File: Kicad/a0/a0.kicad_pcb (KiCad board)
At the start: 2 copper layers, 190 x 100 mm, 73 parts, among them J1 Conn_02x03_Odd_Even, J2 VGA, J4 AudioJack3_SwitchTR, J5 Conn_02x17_Odd_Even, J6 Barrel_Jack_MountingPin, J7 DE9_Plug, J8 DE9_Plug, SW1 SW_Push_45deg, SW10 SW_Push_45deg, SW11 SW_Push_45deg, SW12 SW_Push_45deg, SW13 SW_Push_45deg, SW14 SW_Push_45deg, SW15 SW_Push_45deg, SW16 SW_Push_45deg, SW17 SW_Push_45deg, SW18 SW_Push_45deg, SW19 SW_Push_45deg, SW2 SW_Push_45deg, SW20 SW_Push_45deg, SW21 SW_Push_45deg, SW22 SW_Push_45deg, SW23 SW_Push_45deg, SW24 SW_Push_45deg, SW25 SW_Push_45deg, SW26 SW_Push_45deg, SW27 SW_Push_45deg, SW28 SW_Push_45deg, SW29 SW_Push_45deg, SW3 SW_Push_45deg, SW30 SW_Push_45deg, SW31 SW_Push, SW32 SW_SPDT, SW4 SW_Push_45deg, SW5 SW_Push_45deg, SW6 SW_Push_45deg, SW7 SW_Push_45deg, SW8 SW_Push_45deg, SW9 SW_Push_45deg, U1 74HC590A, U10 74LS541, U11 74LS166, U2 74HC590A, U3 74LS14, U4 74LS174, U5 4520, U6 74LS32, U7 74LS10, U8 CY62256-70PC, U9 28C256, Y1 Crystal

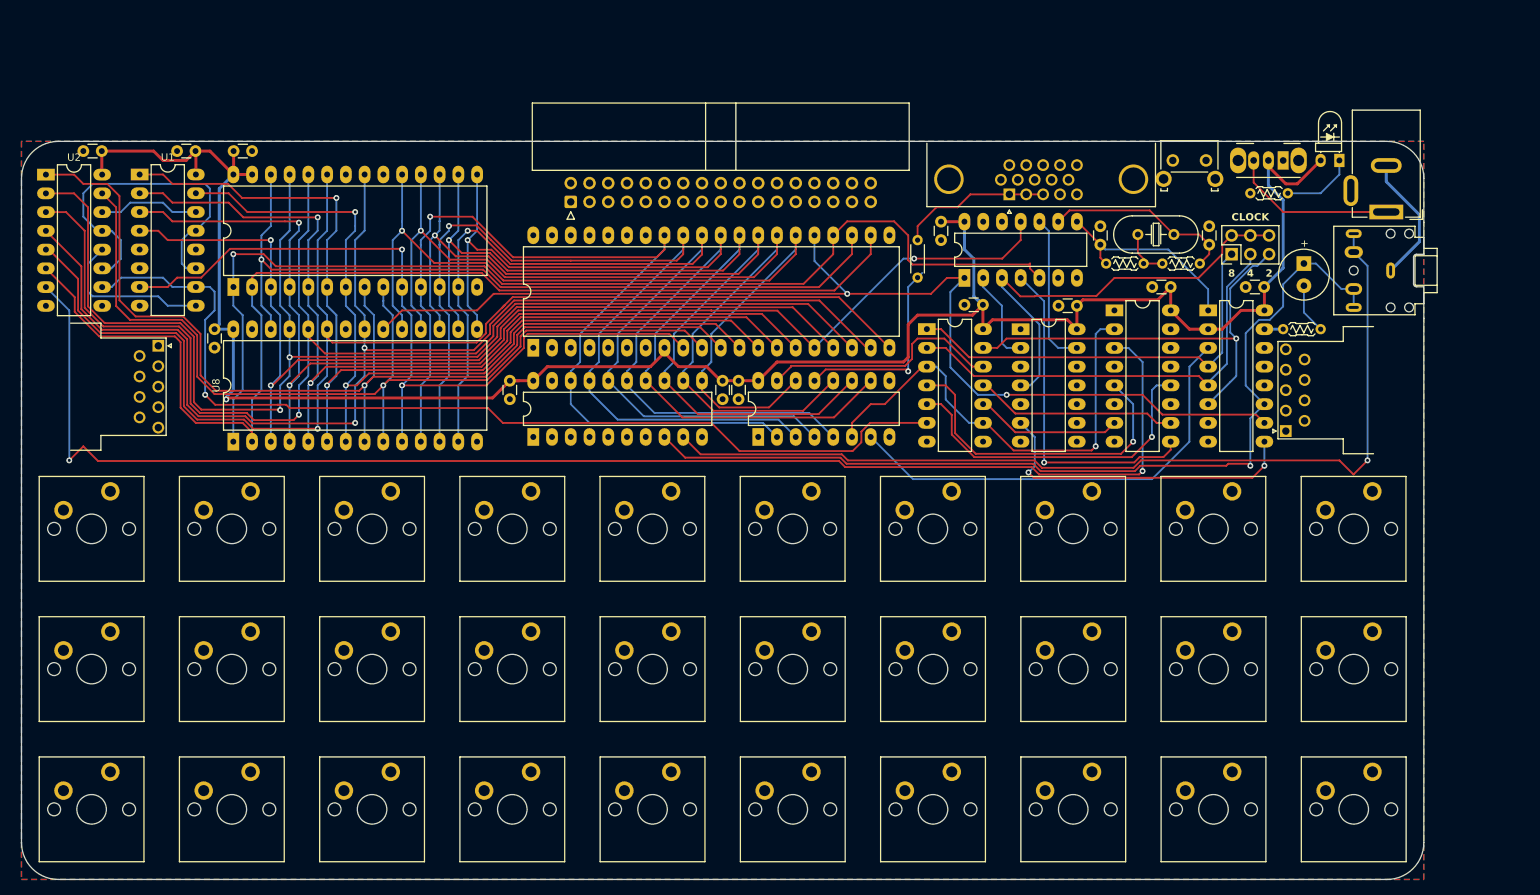
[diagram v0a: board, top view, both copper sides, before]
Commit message: pcb,bios,font  improvements
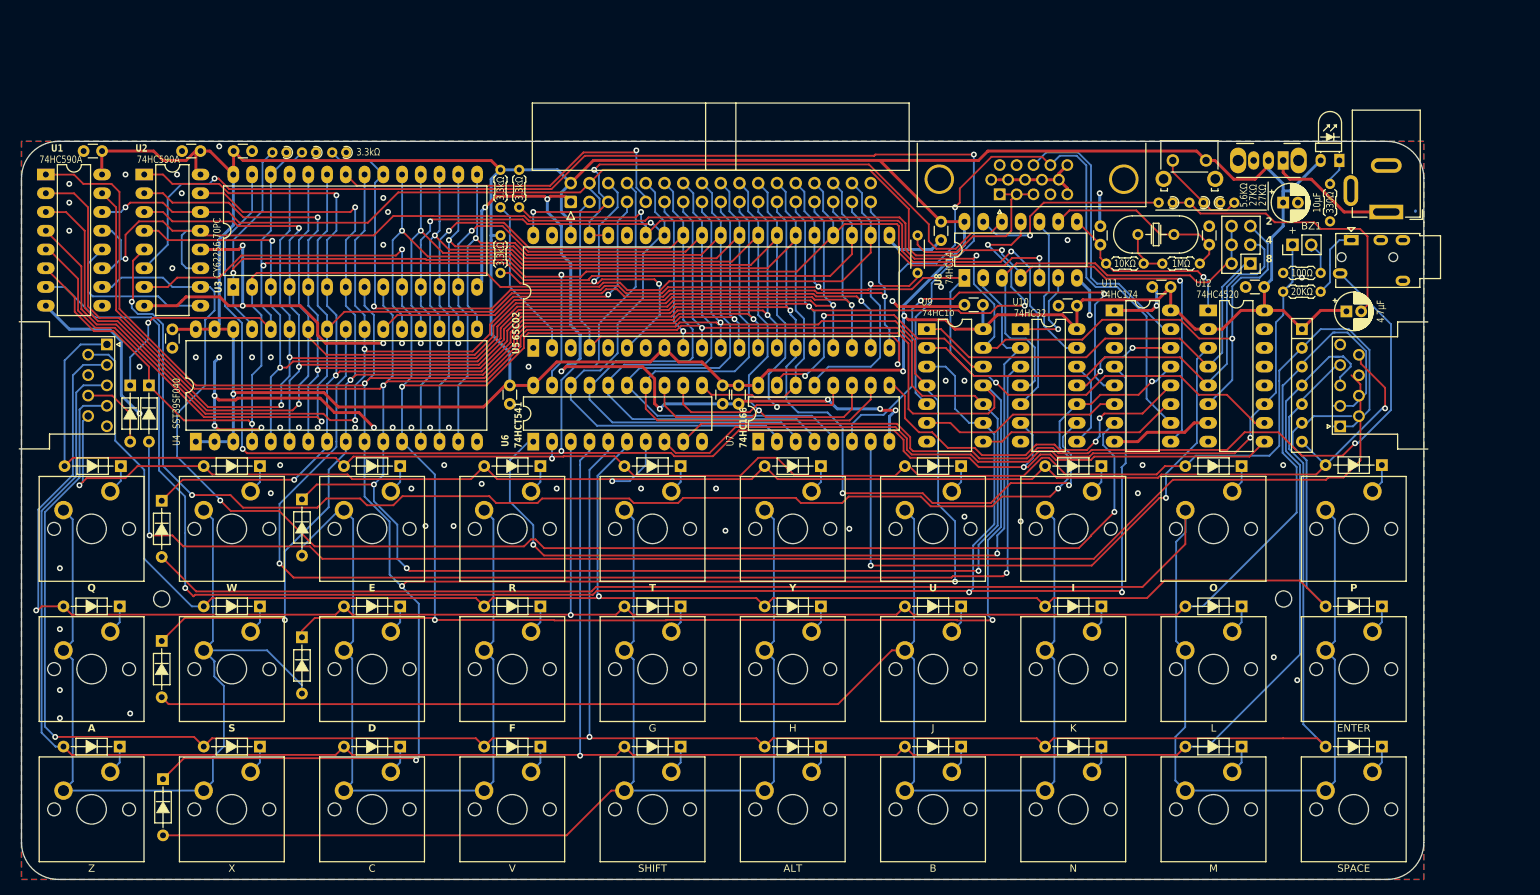
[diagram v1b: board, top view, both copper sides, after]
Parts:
- removed J4: AudioJack3_SwitchTR, Connector_Audio:Jack_3.5mm_CUI_SJ1-3525N_Horizontal
- removed the U9 at (76.2, 62.2)
- added C16: 10µF, PCM_Capacitor_THT_AKL:CP_Radial_D5.0mm_P2.00mm, F.Cu at (218.4, 50.8)
- added C3: 4.7µF, PCM_Capacitor_THT_AKL:CP_Radial_D5.0mm_P2.00mm, F.Cu at (227.0, 65.5)
- added D10: 1N4148, PCM_Diode_THT_AKL:D_DO-35_SOD27_P7.62mm_Horizontal, F.Cu at (174.8, 86.5)
- added D11: 1N4148, PCM_Diode_THT_AKL:D_DO-35_SOD27_P7.62mm_Horizontal, F.Cu at (212.8, 86.5)
- added D12: 1N4148, PCM_Diode_THT_AKL:D_DO-35_SOD27_P7.62mm_Horizontal, F.Cu at (231.8, 86.4)
- added D13: 1N4148, PCM_Diode_THT_AKL:D_DO-35_SOD27_P7.62mm_Horizontal, F.Cu at (193.8, 86.5)
- added D14: 1N4148, PCM_Diode_THT_AKL:D_DO-35_SOD27_P7.62mm_Horizontal, F.Cu at (155.8, 86.5)
- added D15: 1N4148, PCM_Diode_THT_AKL:D_DO-35_SOD27_P7.62mm_Horizontal, F.Cu at (117.8, 86.5)
- added D16: 1N4148, PCM_Diode_THT_AKL:D_DO-35_SOD27_P7.62mm_Horizontal, F.Cu at (79.8, 86.5)
- added D17: 1N4148, PCM_Diode_THT_AKL:D_DO-35_SOD27_P7.62mm_Horizontal, F.Cu at (60.8, 105.5)
- added D18: 1N4148, PCM_Diode_THT_AKL:D_DO-35_SOD27_P7.62mm_Horizontal, F.Cu at (98.8, 105.5)
- added D19: 1N4148, PCM_Diode_THT_AKL:D_DO-35_SOD27_P7.62mm_Horizontal, F.Cu at (136.8, 105.5)
- added D2: 1N4148, PCM_Diode_THT_AKL:D_DO-35_SOD27_P7.62mm_Horizontal, F.Cu at (85.5, 109.7)
- added D20: 1N4148, PCM_Diode_THT_AKL:D_DO-35_SOD27_P7.62mm_Horizontal, F.Cu at (174.8, 105.5)
- added D21: 1N4148, PCM_Diode_THT_AKL:D_DO-35_SOD27_P7.62mm_Horizontal, F.Cu at (212.8, 105.5)
- added D22: 1N4148, PCM_Diode_THT_AKL:D_DO-35_SOD27_P7.62mm_Horizontal, F.Cu at (79.8, 105.5)
- added D23: 1N4148, PCM_Diode_THT_AKL:D_DO-35_SOD27_P7.62mm_Horizontal, F.Cu at (117.8, 105.5)
- added D24: 1N4148, PCM_Diode_THT_AKL:D_DO-35_SOD27_P7.62mm_Horizontal, F.Cu at (155.8, 105.5)
- added D25: 1N4148, PCM_Diode_THT_AKL:D_DO-35_SOD27_P7.62mm_Horizontal, F.Cu at (193.8, 105.5)
- added D26: 1N4148, PCM_Diode_THT_AKL:D_DO-35_SOD27_P7.62mm_Horizontal, F.Cu at (231.8, 105.5)
- added D27: 1N4148, PCM_Diode_THT_AKL:D_DO-35_SOD27_P7.62mm_Horizontal, F.Cu at (60.8, 124.5)
- added D28: 1N4148, PCM_Diode_THT_AKL:D_DO-35_SOD27_P7.62mm_Horizontal, F.Cu at (98.8, 124.5)
- added D29: 1N4148, PCM_Diode_THT_AKL:D_DO-35_SOD27_P7.62mm_Horizontal, F.Cu at (136.8, 124.5)
- added D3: 1N4148, PCM_Diode_THT_AKL:D_DO-35_SOD27_P7.62mm_Horizontal, F.Cu at (85.5, 91.0)
- added D30: 1N4148, PCM_Diode_THT_AKL:D_DO-35_SOD27_P7.62mm_Horizontal, F.Cu at (174.8, 124.5)
- added D31: 1N4148, PCM_Diode_THT_AKL:D_DO-35_SOD27_P7.62mm_Horizontal, F.Cu at (212.8, 124.5)
- added D32: 1N4148, PCM_Diode_THT_AKL:D_DO-35_SOD27_P7.62mm_Horizontal, F.Cu at (79.8, 124.5)
- added D33: 1N4148, PCM_Diode_THT_AKL:D_DO-35_SOD27_P7.62mm_Horizontal, F.Cu at (117.8, 124.5)
- added D34: 1N4148, PCM_Diode_THT_AKL:D_DO-35_SOD27_P7.62mm_Horizontal, F.Cu at (155.8, 124.5)
- added D35: 1N4148, PCM_Diode_THT_AKL:D_DO-35_SOD27_P7.62mm_Horizontal, F.Cu at (193.8, 124.5)
- added D36: 1N4148, PCM_Diode_THT_AKL:D_DO-35_SOD27_P7.62mm_Horizontal, F.Cu at (231.8, 124.5)
- added D37: 1N4148, PCM_Diode_THT_AKL:D_DO-35_SOD27_P7.62mm_Horizontal, F.Cu at (64.8, 75.6)
- added D38: 1N4148, PCM_Diode_THT_AKL:D_DO-35_SOD27_P7.62mm_Horizontal, F.Cu at (62.2, 75.6)
- added D4: 1N4148, PCM_Diode_THT_AKL:D_DO-35_SOD27_P7.62mm_Horizontal, F.Cu at (66.7, 128.9)
- added D5: 1N4148, PCM_Diode_THT_AKL:D_DO-35_SOD27_P7.62mm_Horizontal, F.Cu at (66.5, 110.2)
- added D6: 1N4148, PCM_Diode_THT_AKL:D_DO-35_SOD27_P7.62mm_Horizontal, F.Cu at (66.5, 91.2)
- added D7: 1N4148, PCM_Diode_THT_AKL:D_DO-35_SOD27_P7.62mm_Horizontal, F.Cu at (61.0, 86.5)
- added D8: 1N4148, PCM_Diode_THT_AKL:D_DO-35_SOD27_P7.62mm_Horizontal, F.Cu at (98.8, 86.5)
- added D9: 1N4148, PCM_Diode_THT_AKL:D_DO-35_SOD27_P7.62mm_Horizontal, F.Cu at (136.8, 86.5)
- added H1: MountingHole, MountingHole:MountingHole_2.2mm_M2, F.Cu at (66.5, 104.5)
- added H2: MountingHole, MountingHole:MountingHole_2.2mm_M2, F.Cu at (218.5, 104.5)
- added J3: AudioJack4, Connector_Audio:Jack_3.5mm_PJ320E_Horizontal, F.Cu at (227.7, 55.9)
- added R10: 3.3kΩ, PCM_Resistor_THT_AKL:R_Axial_DIN0204_L3.6mm_D1.6mm_P5.08mm_Horizontal, F.Cu at (114.9, 46.4)
- added R11: 5.6KΩ, PCM_Resistor_THT_US_AKL:R_Axial_DIN0204_L3.6mm_D1.6mm_P1.90mm_Vertical, F.Cu at (203.5, 50.8)
- added R12: 27KΩ, PCM_Resistor_THT_US_AKL:R_Axial_DIN0204_L3.6mm_D1.6mm_P1.90mm_Vertical, F.Cu at (207.6, 50.8)
- added R13: 27KΩ, PCM_Resistor_THT_US_AKL:R_Axial_DIN0204_L3.6mm_D1.6mm_P1.90mm_Vertical, F.Cu at (209.9, 50.8)
- added R14: 20KΩ, PCM_Resistor_THT_AKL:R_Axial_DIN0204_L3.6mm_D1.6mm_P5.08mm_Horizontal, F.Cu at (218.4, 62.9)
- added R15: 3.3kΩ, PCM_Resistor_THT_AKL:R_Axial_DIN0204_L3.6mm_D1.6mm_P5.08mm_Horizontal, F.Cu at (112.4, 55.2)
- added R6: R_Small, PCM_Resistor_THT_AKL:R_Axial_DIN0204_L3.6mm_D1.6mm_P1.90mm_Vertical, F.Cu at (91.5, 44.0)
- added R7: R_Small, PCM_Resistor_THT_AKL:R_Axial_DIN0204_L3.6mm_D1.6mm_P1.90mm_Vertical, F.Cu at (83.4, 44.0)
- added R8: R_Small, PCM_Resistor_THT_AKL:R_Axial_DIN0204_L3.6mm_D1.6mm_P1.90mm_Vertical, F.Cu at (87.4, 44.0)
- added R9: 3.3kΩ, PCM_Resistor_THT_AKL:R_Axial_DIN0204_L3.6mm_D1.6mm_P5.08mm_Horizontal, F.Cu at (112.4, 46.4)
- added RN1: R_Network06, Resistor_THT:R_Array_SIP7, F.Cu at (221.0, 67.9)
- added U4: SST39SF040, Package_DIP:DIP-32_W15.24mm_LongPads, F.Cu at (71.1, 83.2)
- BZ1: footprint Buzzer_Beeper:MagneticBuzzer_Kobitone_254-EMB73-RO -> Connector_PinHeader_2.54mm:PinHeader_1x02_P2.54mm_Vertical
- J6: value Barrel_Jack_MountingPin -> Barrel Jack
- R1: value R -> 1MΩ; footprint PCM_Resistor_THT_US_AKL_Double:R_Axial_DIN0204_L3.6mm_D1.6mm_P5.08mm_Horizontal -> PCM_Resistor_THT_AKL:R_Axial_DIN0204_L3.6mm_D1.6mm_P5.08mm_Horizontal
- R2: value R -> 10KΩ; footprint PCM_Resistor_THT_US_AKL_Double:R_Axial_DIN0204_L3.6mm_D1.6mm_P5.08mm_Horizontal -> PCM_Resistor_THT_AKL:R_Axial_DIN0204_L3.6mm_D1.6mm_P5.08mm_Horizontal
- R4: value R -> 330Ω; footprint PCM_Resistor_THT_US_AKL_Double:R_Axial_DIN0204_L3.6mm_D1.6mm_P5.08mm_Horizontal -> PCM_Resistor_THT_AKL:R_Axial_DIN0204_L3.6mm_D1.6mm_P5.08mm_Horizontal
- R5: value R -> 100Ω; footprint PCM_Resistor_THT_US_AKL_Double:R_Axial_DIN0204_L3.6mm_D1.6mm_P5.08mm_Horizontal -> PCM_Resistor_THT_AKL:R_Axial_DIN0204_L3.6mm_D1.6mm_P5.08mm_Horizontal
- SW1: value SW_Push_45deg -> Q
- SW10: value SW_Push_45deg -> P
- SW11: value SW_Push_45deg -> A
- SW12: value SW_Push_45deg -> S
- SW13: value SW_Push_45deg -> D
- SW14: value SW_Push_45deg -> F
- SW15: value SW_Push_45deg -> G
- SW16: value SW_Push_45deg -> H
- SW17: value SW_Push_45deg -> J
- SW18: value SW_Push_45deg -> K
- SW19: value SW_Push_45deg -> L
- SW2: value SW_Push_45deg -> W
- SW20: value SW_Push_45deg -> ENTER
- SW21: value SW_Push_45deg -> Z
- SW22: value SW_Push_45deg -> X
- SW23: value SW_Push_45deg -> C
- SW24: value SW_Push_45deg -> V
- SW25: value SW_Push_45deg -> SHIFT
- SW26: value SW_Push_45deg -> ALT
- SW27: value SW_Push_45deg -> B
- SW28: value SW_Push_45deg -> N
- SW29: value SW_Push_45deg -> M
- SW3: value SW_Push_45deg -> E
- SW30: value SW_Push_45deg -> SPACE
- SW4: value SW_Push_45deg -> R
- SW5: value SW_Push_45deg -> T
- SW6: value SW_Push_45deg -> Y
- SW7: value SW_Push_45deg -> U
- SW8: value SW_Push_45deg -> I
- SW9: value SW_Push_45deg -> O
- U10: renamed from U6; value 74LS32 -> 74HC32
- U11: renamed from U4; value 74LS174 -> 74HC174
- U12: renamed from U5; value 4520 -> 74HC4520
- U5: renamed from U12; value ~ -> 65C02
- U6: renamed from U10; value 74LS541 -> 74HCT541
- U7: renamed from U11; value 74LS166 -> 74HC166
- U8: renamed from U3; value 74LS14 -> 74HC14
- U9: renamed from U7; value 74LS10 -> 74HC10
- Y1: value Crystal -> 32Mhz
- moved J8 160.5 mm to (226.2, 81.1), turned to 90 degrees
- moved J7 160.2 mm to (59.1, 70.0), turned to -90 degrees
- moved U3 21.0 mm to (76.2, 62.2)
- moved R4 11.4 mm to (224.8, 53.3), turned to 90 degrees
- moved R5 7.62 mm to (223.5, 60.3)
- moved C7 5.72 mm to (67.9, 70.5)
- moved BZ1 2.97 mm to (219.7, 56.5), turned to 90 degrees
- moved J1 2.84 mm to (214.0, 59.1), turned to 180 degrees
- moved J2 1.31 mm to (180.0, 49.7)
- moved C5 0.67 mm to (69.3, 43.8)
- moved U6 0.64 mm to (116.8, 83.2)
- moved U7 0.64 mm to (147.3, 83.2)
- moved R3 0.63 mm to (168.9, 60.3)
- moved C10 0.63 mm to (144.7, 78.1)
- moved C8 0.63 mm to (113.7, 78.1)
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- renumbered U2 to U1, U1 to U2, U8 to U3
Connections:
- C10 pad 1: unconnected-(C10-Pad1) -> GND
- C11 pad 1: unconnected-(C11-Pad1) -> GND
- C12 pad 1: unconnected-(C12-Pad1) -> GND
- C13 pad 1: unconnected-(C13-Pad1) -> GND
- C14 pad 1: unconnected-(C14-Pad1) -> GND
- C15 pad 1: unconnected-(C15-Pad1) -> GND
- C4 pad 1: unconnected-(C4-Pad1) -> GND
- C5 pad 1: unconnected-(C5-Pad1) -> GND
- C6 pad 1: unconnected-(C6-Pad1) -> GND
- C7 pad 1: unconnected-(C7-Pad1) -> GND
- C8 pad 1: unconnected-(C8-Pad1) -> GND
- J5 pad 1: unconnected-(J5-Pin_1-Pad1) -> GND
- J5 pad 10: unconnected-(J5-Pin_10-Pad10) -> /D0
- J5 pad 11: unconnected-(J5-Pin_11-Pad11) -> /A0
- J5 pad 12: unconnected-(J5-Pin_12-Pad12) -> /D1
- J5 pad 13: unconnected-(J5-Pin_13-Pad13) -> /A1
- J5 pad 14: unconnected-(J5-Pin_14-Pad14) -> /D2
- J5 pad 15: unconnected-(J5-Pin_15-Pad15) -> /A2
- J5 pad 16: unconnected-(J5-Pin_16-Pad16) -> /D3
- J5 pad 17: unconnected-(J5-Pin_17-Pad17) -> /A3
- J5 pad 18: unconnected-(J5-Pin_18-Pad18) -> /D4
- J5 pad 19: unconnected-(J5-Pin_19-Pad19) -> /A4
- J5 pad 2: unconnected-(J5-Pin_2-Pad2) -> VCC
- J5 pad 20: unconnected-(J5-Pin_20-Pad20) -> /D5
- J5 pad 21: unconnected-(J5-Pin_21-Pad21) -> /A5
- J5 pad 22: unconnected-(J5-Pin_22-Pad22) -> /D6
- J5 pad 23: unconnected-(J5-Pin_23-Pad23) -> /A6
- J5 pad 24: unconnected-(J5-Pin_24-Pad24) -> /D7
- J5 pad 25: unconnected-(J5-Pin_25-Pad25) -> /A7
- J5 pad 26: unconnected-(J5-Pin_26-Pad26) -> /A15
- J5 pad 27: unconnected-(J5-Pin_27-Pad27) -> /A8
- J5 pad 28: unconnected-(J5-Pin_28-Pad28) -> /A14
- J5 pad 29: unconnected-(J5-Pin_29-Pad29) -> /A9
- J5 pad 3: unconnected-(J5-Pin_3-Pad3) -> /~{VSYNC}
- J5 pad 30: unconnected-(J5-Pin_30-Pad30) -> /A13
- J5 pad 31: unconnected-(J5-Pin_31-Pad31) -> /A10
- J5 pad 32: unconnected-(J5-Pin_32-Pad32) -> /A12
- J5 pad 33: unconnected-(J5-Pin_33-Pad33) -> /A11
- J5 pad 34: unconnected-(J5-Pin_34-Pad34) -> GND
- J5 pad 4: unconnected-(J5-Pin_4-Pad4) -> ø2
- J5 pad 5: unconnected-(J5-Pin_5-Pad5) -> /~{RESEŦ}
- J5 pad 6: unconnected-(J5-Pin_6-Pad6) -> /~{NMI}
- J5 pad 7: unconnected-(J5-Pin_7-Pad7) -> /ROMDIS
- J5 pad 8: unconnected-(J5-Pin_8-Pad8) -> /~{WR}
- J5 pad 9: unconnected-(J5-Pin_9-Pad9) -> /RAMDIS
- J6 pad 1: Net-(SW32-C) -> Net-(SW32-A)
- J7 pad 1: unconnected-(J7-Pad1) -> /HROW 0
- J7 pad 2: unconnected-(J7-Pad2) -> /HROW 1
- J7 pad 3: unconnected-(J7-Pad3) -> /HROW 2
- J7 pad 4: unconnected-(J7-Pad4) -> /HROW 3
- J7 pad 6: unconnected-(J7-Pad6) -> /HROW 4
- J7 pad 8: unconnected-(J7-Pad8) -> Net-(D38-A)
- J7 pad 9: unconnected-(J7-Pad9) -> /HROW 5
- J8 pad 1: unconnected-(J8-Pad1) -> /HROW 0
- J8 pad 2: unconnected-(J8-Pad2) -> /HROW 1
- J8 pad 3: unconnected-(J8-Pad3) -> /HROW 2
- J8 pad 4: unconnected-(J8-Pad4) -> /HROW 3
- J8 pad 6: unconnected-(J8-Pad6) -> /HROW 4
- J8 pad 8: unconnected-(J8-Pad8) -> Net-(D37-A)
- J8 pad 9: unconnected-(J8-Pad9) -> /HROW 5
- SW1 pad 1: unconnected-(SW1-Pad1) -> /COL 0
- SW1 pad 2: unconnected-(SW1-Pad2) -> Net-(D7-K)
- SW10 pad 1: unconnected-(SW10-Pad1) -> /COL 4
- SW10 pad 2: unconnected-(SW10-Pad2) -> Net-(D12-K)
- SW11 pad 1: unconnected-(SW11-Pad1) -> /COL 0
- SW11 pad 2: unconnected-(SW11-Pad2) -> Net-(D17-K)
- SW12 pad 1: unconnected-(SW12-Pad1) -> /COL 0
- SW12 pad 2: unconnected-(SW12-Pad2) -> Net-(D22-K)
- SW13 pad 1: unconnected-(SW13-Pad1) -> /COL 1
- SW13 pad 2: unconnected-(SW13-Pad2) -> Net-(D18-K)
- SW14 pad 1: unconnected-(SW14-Pad1) -> /COL 1
- SW14 pad 2: unconnected-(SW14-Pad2) -> Net-(D23-K)
- SW15 pad 1: unconnected-(SW15-Pad1) -> /COL 2
- SW15 pad 2: unconnected-(SW15-Pad2) -> Net-(D19-K)
- SW16 pad 1: unconnected-(SW16-Pad1) -> /COL 2
- SW16 pad 2: unconnected-(SW16-Pad2) -> Net-(D24-K)
- SW17 pad 1: unconnected-(SW17-Pad1) -> /COL 3
- SW17 pad 2: unconnected-(SW17-Pad2) -> Net-(D20-K)
- SW18 pad 1: unconnected-(SW18-Pad1) -> /COL 3
- SW18 pad 2: unconnected-(SW18-Pad2) -> Net-(D25-K)
- SW19 pad 1: unconnected-(SW19-Pad1) -> /COL 4
- SW19 pad 2: unconnected-(SW19-Pad2) -> Net-(D21-K)
- SW2 pad 1: unconnected-(SW2-Pad1) -> /COL 0
- SW2 pad 2: unconnected-(SW2-Pad2) -> Net-(D16-K)
- SW20 pad 1: unconnected-(SW20-Pad1) -> /COL 4
- SW20 pad 2: unconnected-(SW20-Pad2) -> Net-(D26-K)
- SW21 pad 1: unconnected-(SW21-Pad1) -> /COL 0
- SW21 pad 2: unconnected-(SW21-Pad2) -> Net-(D27-K)
- SW22 pad 1: unconnected-(SW22-Pad1) -> /COL 0
- SW22 pad 2: unconnected-(SW22-Pad2) -> Net-(D32-K)
- SW23 pad 1: unconnected-(SW23-Pad1) -> /COL 1
- SW23 pad 2: unconnected-(SW23-Pad2) -> Net-(D28-K)
- SW24 pad 1: unconnected-(SW24-Pad1) -> /COL 1
- SW24 pad 2: unconnected-(SW24-Pad2) -> Net-(D33-K)
- SW25 pad 1: unconnected-(SW25-Pad1) -> /COL 2
- SW25 pad 2: unconnected-(SW25-Pad2) -> Net-(D29-K)
- SW26 pad 1: unconnected-(SW26-Pad1) -> /COL 2
- SW26 pad 2: unconnected-(SW26-Pad2) -> Net-(D34-K)
- SW27 pad 1: unconnected-(SW27-Pad1) -> /COL 3
- SW27 pad 2: unconnected-(SW27-Pad2) -> Net-(D30-K)
- SW28 pad 1: unconnected-(SW28-Pad1) -> /COL 3
- SW28 pad 2: unconnected-(SW28-Pad2) -> Net-(D35-K)
- SW29 pad 1: unconnected-(SW29-Pad1) -> /COL 4
- SW29 pad 2: unconnected-(SW29-Pad2) -> Net-(D31-K)
- SW3 pad 1: unconnected-(SW3-Pad1) -> /COL 1
- SW3 pad 2: unconnected-(SW3-Pad2) -> Net-(D8-K)
- SW30 pad 1: unconnected-(SW30-Pad1) -> /COL 4
- SW30 pad 2: unconnected-(SW30-Pad2) -> Net-(D36-K)
- SW31 pad 1: unconnected-(SW31-Pad1) -> Net-(R12-Pad1)
- SW31 pad 2: unconnected-(SW31-Pad2) -> VCC
- SW32 pad 1: unconnected-(SW32-A-Pad1) -> Net-(SW32-A)
- SW32 pad 3: Net-(SW32-C) -> unconnected-(SW32-C-Pad3)
- SW4 pad 1: unconnected-(SW4-Pad1) -> /COL 1
- SW4 pad 2: unconnected-(SW4-Pad2) -> Net-(D15-K)
- SW5 pad 1: unconnected-(SW5-Pad1) -> /COL 2
- SW5 pad 2: unconnected-(SW5-Pad2) -> Net-(D9-K)
- SW6 pad 1: unconnected-(SW6-Pad1) -> /COL 2
- SW6 pad 2: unconnected-(SW6-Pad2) -> Net-(D14-K)
- SW7 pad 1: unconnected-(SW7-Pad1) -> /COL 3
- SW7 pad 2: unconnected-(SW7-Pad2) -> Net-(D10-K)
- SW8 pad 1: unconnected-(SW8-Pad1) -> /COL 3
- SW8 pad 2: unconnected-(SW8-Pad2) -> Net-(D13-K)
- SW9 pad 1: unconnected-(SW9-Pad1) -> /COL 4
- SW9 pad 2: unconnected-(SW9-Pad2) -> Net-(D11-K)
- U10 pad 7: unconnected-(U6E-GND-Pad7) -> GND
- U11 pad 10: /V2' -> /~{VSYNC}
- U11 pad 11: /A0 -> Net-(U11-D3)
- U11 pad 12: /V1' -> /H32'
- U11 pad 13: /V1 -> /H32
- U11 pad 2: /V512' -> unconnected-(U11-Q0-Pad2)
- U11 pad 3: /V512 -> unconnected-(U11-D0-Pad3)
- U11 pad 4: /A2 -> /V512
- U11 pad 5: /V8' -> /V512'
- U11 pad 6: /A1 -> Net-(U11-D2)
- U11 pad 7: /V4' -> /~{MRC}
- U11 pad 8: unconnected-(U4-GND-Pad8) -> GND
- U12 pad 8: unconnected-(U5C-VSS-Pad8) -> GND
- U3 pad 14: unconnected-(U8-GND-Pad14) -> GND
- U5 pad 2: unconnected-(U12-RDY-Pad2) -> Net-(U5-RDY)
- U5 pad 21: unconnected-(U12-VSS-Pad21) -> GND
- U5 pad 34: unconnected-(U12-R/~{W}-Pad34) -> /r/~{w}
- U5 pad 36: unconnected-(U12-BE-Pad36) -> ø2
- U5 pad 37: unconnected-(U12-ø0-Pad37) -> ø2
- U5 pad 38: unconnected-(U12-~{SO}-Pad38) -> VCC
- U5 pad 4: unconnected-(U12-~{IRQ}-Pad4) -> /~{VSYNC}
- U5 pad 40: unconnected-(U12-~{RESET}-Pad40) -> /~{RESEŦ}
- U5 pad 6: unconnected-(U12-~{NMI}-Pad6) -> /~{NMI}
- U6 pad 10: unconnected-(U10-GND-Pad10) -> GND
- U6 pad 2: unconnected-(U10-A0-Pad2) -> /HROW 0
- U6 pad 3: unconnected-(U10-A1-Pad3) -> /HROW 1
- U6 pad 4: unconnected-(U10-A2-Pad4) -> /HROW 2
- U6 pad 5: unconnected-(U10-A3-Pad5) -> /HROW 3
- U6 pad 6: unconnected-(U10-A4-Pad6) -> /HROW 4
- U6 pad 7: unconnected-(U10-A5-Pad7) -> /HROW 5
- U8 pad 12: unconnected-(U3-Pad12) -> /~{RESEŦ}
- U8 pad 13: unconnected-(U3-Pad13) -> Net-(R11-Pad2)
- U8 pad 7: unconnected-(U3G-GND-Pad7) -> GND
- U9 pad 10: /V4' -> /A1
- U9 pad 11: /V2' -> /A0
- U9 pad 3: /V512' -> /V512
- U9 pad 4: /V8' -> /A2
- U9 pad 5: /V1' -> /V1
- U9 pad 6: /~{MRC} -> Net-(U11-D2)
- U9 pad 7: unconnected-(U7D-GND-Pad7) -> GND
- U9 pad 8: /~{VSYNC} -> Net-(U11-D3)
- U9 pad 9: /V512' -> /V512
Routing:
- net /HROW 2: track 0.00 -> 327.0 mm, vias 0 -> 1
- net /HROW 3: track 0.00 -> 326.0 mm, vias 0 -> 2
- net /HROW 1: track 0.00 -> 288.0 mm, vias 0 -> 2
- net GND: track 20.2 -> 286.4 mm, vias 0 -> 78
- net /HROW 4: track 0.00 -> 258.2 mm, vias 0 -> 1
- net /COL 4: track 0.00 -> 247.1 mm
- net /HROW 0: track 0.00 -> 238.1 mm, vias 0 -> 1
- net /A2: track 142.7 -> 379.7 mm, vias 1 -> 5
- net /A0: track 107.4 -> 339.5 mm, vias 2 -> 5
- net VCC: track 281.4 -> 511.9 mm, vias 1 -> 3
- net /HROW 5: track 0.00 -> 219.3 mm, vias 0 -> 3
- net /COL 3: track 0.00 -> 203.2 mm
- net Net-(D37-A): track 0.00 -> 195.7 mm, vias 0 -> 1
- net /A1: track 131.0 -> 326.3 mm, vias 1 -> 5
- net /~{WR}: track 44.1 -> 234.9 mm, vias 2 -> 3
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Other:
- outline, holes or cut-outs redrawn
- board text added: "+"
- board text added: "3.3kΩ"
- board text removed: "CLOCK"

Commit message: update pcb
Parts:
- moved J7 0.70 mm to (58.5, 70.5)
- moved J8 0.30 mm to (226.5, 81.1)
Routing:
- net /AUDIN: track 127.1 -> 134.3 mm
- net /HROW 0: track 238.1 -> 240.8 mm
- net /HROW 5: track 219.3 -> 221.5 mm
- net Net-(D37-A): track 195.7 -> 197.5 mm
- net /HROW 4: track 258.2 -> 260.0 mm
- net /HROW 1: track 288.0 -> 289.6 mm
- net GND: vias 78 -> 81

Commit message: file update
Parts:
- removed R10, R15: 3.3kΩ, PCM_Resistor_THT_AKL:R_Axial_DIN0204_L3.6mm_D1.6mm_P5.08mm_Horizontal
- removed R6, R7, R8: R_Small, PCM_Resistor_THT_AKL:R_Axial_DIN0204_L3.6mm_D1.6mm_P1.90mm_Vertical
- added R18: R_Small, PCM_Resistor_THT_AKL:R_Axial_DIN0204_L3.6mm_D1.6mm_P1.90mm_Vertical, F.Cu at (89.3, 43.8)
- added RN2: R_Network08, Resistor_THT:R_Array_SIP9, F.Cu at (219.1, 62.9)
- C1, C2: value C_Small -> 33pF
- R14, R5: footprint PCM_Resistor_THT_AKL:R_Axial_DIN0204_L3.6mm_D1.6mm_P5.08mm_Horizontal -> PCM_Resistor_THT_US_AKL:R_Axial_DIN0204_L3.6mm_D1.6mm_P1.90mm_Vertical
- R3: footprint Resistor_THT:R_Axial_DIN0204_L3.6mm_D1.6mm_P5.08mm_Horizontal -> PCM_Resistor_THT_AKL:R_Axial_DIN0204_L3.6mm_D1.6mm_P5.08mm_Horizontal
- RN1: value R_Network06 -> R_Network08; footprint Resistor_THT:R_Array_SIP7 -> Resistor_THT:R_Array_SIP9
- U5: value 65C02 -> W65C02SxP; footprint Package_DIP:DIP-40_W15.24mm_LongPads -> Package_DIP:DIP-40_W15.24mm
- moved J1 42.5 mm to (171.5, 59.1), turned to 90 degrees
- moved C2 21.4 mm to (215.1, 56.4), turned to -90 degrees
- moved R2 11.0 mm to (209.2, 53.8), turned to 0 degrees
- moved C1 8.40 mm to (200.0, 56.4), turned to -90 degrees
- moved R1 7.62 mm to (201.6, 53.8), turned to 0 degrees
- moved U8 6.35 mm to (181.6, 61.0)
- moved R14 6.06 mm to (223.2, 59.1), turned to 180 degrees
- moved RN1 5.43 mm to (222.9, 62.9)
- moved C11 4.60 mm to (175.9, 53.3), turned to 0 degrees
- moved R5 3.83 mm to (223.2, 56.5)
- moved Y1 3.05 mm to (205.1, 57.8), turned to 0 degrees
- moved BZ1 2.84 mm to (218.4, 59.1), turned to 180 degrees
- moved R9 2.54 mm to (114.9, 46.4)
- moved R3 0.63 mm to (168.3, 60.3)
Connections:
- net Net-(J3-PadT) renamed /DataOut
- BZ1 pad 1: /BEEP -> /Speaker
- BZ1 pad 2: Net-(BZ1--) -> GND
- D37 pad 1: /A12 -> /A11
- D38 pad 1: /A13 -> /A12
- J5 pad 10: /D0 -> /r/~{w}
- J5 pad 12: /D1 -> /D0
- J5 pad 14: /D2 -> /D1
- J5 pad 16: /D3 -> /D2
- J5 pad 18: /D4 -> /D3
- J5 pad 20: /D5 -> /D4
- J5 pad 22: /D6 -> /D5
- J5 pad 24: /D7 -> /D6
- J5 pad 26: /A15 -> /D7
- J5 pad 28: /A14 -> /A15
- J5 pad 3: /~{VSYNC} -> /M16
- J5 pad 30: /A13 -> /A14
- J5 pad 32: /A12 -> /A13
- J5 pad 34: GND -> /A12
- J5 pad 5: /~{RESEŦ} -> /~{RESET}
- J5 pad 7: /ROMDIS -> /RAMHIDE
- J5 pad 8: /~{WR} -> /~{A15}
- J5 pad 9: /RAMDIS -> /~{A13}
- R5 pad 1: Net-(BZ1--) -> /BEEP
- R5 pad 2: GND -> /Speaker
- RN1 pad 2: /HROW 0 -> /r/~{w}
- RN1 pad 3: /HROW 1 -> /NMI
- RN1 pad 4: /HROW 2 -> /HROW 0
- RN1 pad 5: /HROW 3 -> /HROW 1
- RN1 pad 6: /HROW 4 -> /HROW 2
- RN1 pad 7: /HROW 5 -> /HROW 3
- U10 pad 1: Net-(U10-Pad1) -> /H32
- U10 pad 2: Net-(U6-G1) -> /H32'
- U10 pad 3: /~{UPPER} -> Net-(U7-Clr)
- U10 pad 8: Net-(U10-Pad12) -> Net-(U10-Pad13)
- U10 pad 9: /A6 -> /A7
- U2 pad 6: /V1 -> /A1
- U3 pad 22: /RAMDIS -> /RAMHIDE
- U4 pad 22: /ROMDIS -> /~{A13}
- U4 pad 24: /~{UPPER} -> /~{A15}
- U5 pad 40: /~{RESEŦ} -> /~{RESET}
- U6 pad 1: Net-(U6-G1) -> /~{A15}
- U7 pad 9: /H32' -> Net-(U7-Clr)
- U8 pad 10: Net-(U10-Pad13) -> /~{RESET}
- U8 pad 11: /A7 -> Net-(R11-Pad2)
- U8 pad 12: /~{RESEŦ} -> ø2
- U8 pad 13: Net-(R11-Pad2) -> /ø1
- U8 pad 2: Net-(U6-G1) -> /~{A15}
- U8 pad 3: /ø1 -> /A6
- U8 pad 4: ø2 -> Net-(U10-Pad12)
- U8 pad 5: /A14 -> /A13
- U8 pad 6: Net-(U10-Pad1) -> /~{A13}
- U9 pad 1: /M8 -> /V512
- U9 pad 10: /A1 -> /A2
- U9 pad 12: /~{sload} -> Net-(U11-D2)
- U9 pad 13: /M2 -> /A1
- U9 pad 2: /M4 -> /A2
- U9 pad 3: /V512 -> /M8
- U9 pad 4: /A2 -> /M4
- U9 pad 5: /V1 -> /M2
- U9 pad 6: Net-(U11-D2) -> /~{sload}
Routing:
- net /HROW 2: track 327.0 -> 0.00 mm, vias 1 -> 0
- net /HROW 3: track 325.9 -> 0.00 mm, vias 2 -> 0
- net /A2: track 379.7 -> 65.4 mm, vias 5 -> 1
- net VCC: track 511.9 -> 220.9 mm, vias 3 -> 1
- net /HROW 1: track 289.6 -> 0.00 mm, vias 2 -> 0
- net GND: track 286.4 -> 0.00 mm, vias 81 -> 0
- net /A0: track 339.5 -> 71.5 mm, vias 5 -> 1
- net /A1: track 326.3 -> 63.0 mm, vias 5 -> 0
- net /HROW 4: track 260.0 -> 0.00 mm, vias 1 -> 0
- net /V512: track 253.2 -> 0.00 mm, vias 3 -> 0
- net /COL 4: track 247.1 -> 0.00 mm
- net /HROW 0: track 240.8 -> 0.00 mm, vias 1 -> 0
- net /~{WR}: track 234.9 -> 0.00 mm, vias 3 -> 0
- net /HROW 5: track 221.5 -> 0.00 mm, vias 3 -> 0
- net /COL 3: track 203.2 -> 0.00 mm
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
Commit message: Update pcb and readme
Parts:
- removed R18: R_Small, PCM_Resistor_THT_AKL:R_Axial_DIN0204_L3.6mm_D1.6mm_P1.90mm_Vertical
- removed R9: 3.3kΩ, PCM_Resistor_THT_AKL:R_Axial_DIN0204_L3.6mm_D1.6mm_P5.08mm_Horizontal
- added H3: MountingHole_Pad, MountingHole:MountingHole_2.2mm_M2_ISO7380_Pad, F.Cu at (74.3, 111.6)
- added H4: MountingHole_Pad, MountingHole:MountingHole_2.2mm_M2_ISO7380_Pad, F.Cu at (226.3, 111.6)
- added RN3: R_Network04, Resistor_THT:R_Array_SIP5, F.Cu at (91.6, 31.9)
- BZ1: footprint Connector_PinHeader_2.54mm:PinHeader_1x02_P2.54mm_Vertical -> Buzzer_Beeper:MagneticBuzzer_Kingstate_KCG0601
- C1: value 33pF -> 22pF
- C2: value 33pF -> 27pF
- D1: footprint PCM_LED_THT_AKL_Double:LED_D3.0mm_Horizontal_O1.27mm_Z2.0mm_IRGrey -> LED_THT:LED_D3.0mm
- H1, H2: value MountingHole -> MountingHole_Pad; footprint MountingHole:MountingHole_2.2mm_M2 -> MountingHole:MountingHole_2.2mm_M2_ISO7380_Pad
- J7, J8: footprint Connector_Dsub:DSUB-9_Male_Horizontal_P2.77x2.54mm_EdgePinOffset9.40mm -> Smal:DSUB9-Atari
- R2: value 10KΩ -> 180Ω
- RN2: value R_Network08 -> R_Network04; footprint Resistor_THT:R_Array_SIP9 -> Resistor_THT:R_Array_SIP5
- SW1, SW10, SW11, SW12, SW13, SW14, SW15, SW16, SW17, SW18, SW19, SW2, SW20, SW21, SW22, SW23, SW24, SW25, SW26, SW27, SW28, SW29, SW3, SW30, SW4, SW5, SW6, SW7, SW8, SW9: footprint PCM_Switch_Keyboard_Cherry_MX:SW_Cherry_MX_PCB_1.00u -> Smal:SW_Redragon_MX_LowProfile_PCB_1.00u_Other
- U3: value CY62256-70PC -> 62256
- moved H1 162.7 mm to (226.2, 73.6)
- moved H2 147.5 mm to (74.3, 73.6)
- moved RN2 116.4 mm to (106.8, 31.9), turned to 0 degrees
- moved D3 29.0 mm to (111.9, 79.1)
- moved D2 28.7 mm to (111.9, 98.6)
- moved C3 26.7 mm to (229.1, 38.9), turned to 180 degrees
- moved R3 20.0 mm to (174.8, 41.4), turned to 0 degrees
- moved C8 18.1 mm to (120.2, 61.1), turned to -90 degrees
- moved BZ1 17.4 mm to (229.5, 45.6)
- moved C10 17.4 mm to (148.9, 61.2), turned to -90 degrees
- moved C16 17.0 mm to (235.1, 54.1)
- moved C2 16.3 mm to (221.9, 41.6)
- moved Y1 16.2 mm to (211.7, 43.0)
- moved C1 16.2 mm to (206.6, 41.6)
- moved D19 15.9 mm to (144.6, 91.6)
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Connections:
- C2 pad 1: Net-(U12A-CK) -> Net-(C2-Pad1)
- J2 pad 13: /~{HSYNC} -> /~{HSYNC}**
- J2 pad 9: GND -> VCC
- J3 pad R1: GND -> unconnected-(J3-PadR1)
- J3 pad R2: unconnected-(J3-PadR2) -> GND
- J3 pad S: /AUDIN -> /DataOut
- J3 pad T: /DataOut -> /AUDIN
- J5 pad 4: ø2 -> /ø2
- R1 pad 2: Net-(R1-Pad2) -> Net-(U12A-CK)
- R13 pad 1: GND -> Net-(R12-Pad1)
- R13 pad 2: Net-(R12-Pad1) -> GND
- R2 pad 1: Net-(R1-Pad2) -> Net-(C2-Pad1)
- RN1 pad 2: /r/~{w} -> /Speaker
- RN1 pad 3: /NMI -> /DataOut
- RN1 pad 4: /HROW 0 -> /HROW 5
- RN1 pad 5: /HROW 1 -> /HROW 3
- RN1 pad 7: /HROW 3 -> /HROW 1
- RN1 pad 9: /HROW 5 -> /HROW 0
- RN2 pad 1: GND -> VCC
- RN2 pad 2: unconnected-(RN2-R1-Pad2) -> /~{NMI}
- RN2 pad 3: /Speaker -> /r/~{w}
- RN2 pad 4: /DataOut -> /RDY
- RN2 pad 5: /A13 -> /~{SO}
- U1 pad 11: /M2 -> /~{sload}
- U1 pad 13: /M2 -> /~{sload}
- U1 pad 14: ø2 -> /ø2
- U10 pad 11: Net-(U11-D5) -> Net-(U11-D3)
- U11 pad 10: /~{VSYNC} -> /~{HSYNC}
- U11 pad 12: /H32' -> /~{HSYNC}*
- U11 pad 13: /H32 -> /~{HSYNC}
- U11 pad 14: Net-(U11-D5) -> /~{HSYNC}*
- U11 pad 15: /~{HSYNC} -> /~{HSYNC}**
- U11 pad 2: unconnected-(U11-Q0-Pad2) -> /H32'
- U11 pad 3: unconnected-(U11-D0-Pad3) -> /H32
- U11 pad 4: /V512 -> Net-(U11-D1)
- U11 pad 5: /V512' -> /~{MRC}
- U11 pad 7: /~{MRC} -> /~{VSYNC}
- U11 pad 9: ø2 -> /~{sload}
- U2 pad 10: /~{MRC} -> VCC
- U2 pad 11: /M2 -> /~{sload}
- U2 pad 13: /M2 -> /~{sload}
- U2 pad 14: ø2 -> /ø2
- U2 pad 6: /A1 -> unconnected-(U2-Q6-Pad6)
- U4 pad 28: /A13 -> VCC
- U4 pad 29: /A14 -> VCC
- U5 pad 2: Net-(U5-RDY) -> /RDY
- U5 pad 36: ø2 -> /ø2
- U5 pad 37: ø2 -> /ø2
- U5 pad 38: VCC -> /~{SO}
- U7 pad 6: /V512' -> GND
- U8 pad 12: ø2 -> /ø2
- U9 pad 12: Net-(U11-D2) -> Net-(U11-D1)
- U9 pad 8: Net-(U11-D3) -> Net-(U11-D2)
- Y1 pad 2: Net-(R1-Pad2) -> Net-(C2-Pad1)
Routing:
- net /HROW 2: track 0.00 -> 318.6 mm, vias 0 -> 2
- net /HROW 3: track 0.00 -> 310.2 mm, vias 0 -> 2
- net /COL 4: track 0.00 -> 283.6 mm
- net /HROW 4: track 0.00 -> 280.5 mm, vias 0 -> 3
- net /HROW 1: track 0.00 -> 259.0 mm, vias 0 -> 3
- net /COL 3: track 0.00 -> 238.8 mm
- net Net-(D37-A): track 0.00 -> 227.5 mm, vias 0 -> 2
- net /A2: track 65.4 -> 288.2 mm, vias 1 -> 4
- net /~{MRC}: track 0.00 -> 216.6 mm, vias 0 -> 2
- net GND: track 0.00 -> 213.7 mm, vias 0 -> 124
- net /HROW 5: track 0.00 -> 211.7 mm, vias 0 -> 1
- net /HROW 0: track 0.00 -> 206.6 mm, vias 0 -> 3
- net /~{WR}: track 0.00 -> 205.9 mm, vias 0 -> 2
- net /COL 2: track 0.00 -> 203.4 mm
- net /~{sload}: track 0.00 -> 191.8 mm, vias 0 -> 2
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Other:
- board text added: "27C256 28C64"
- board text added: "CPU"
- board text added: "CPU and Video Logic"
- board text added: "Clock Div/Beeper"
- board text added: "Input Register"
- board text added: "MicroMicro v0 - Dec 2024"
- board text added: "Pixel Shifter"
- board text added: "RAM and ROM"
- board text added: "System Clock"
- board text added: "Video Counters"
- board text added: "github.com/smaldragon/MicroMicro"
- board text removed: "3.3kΩ"

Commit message: Updated PCBs and Code
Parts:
- SW21: value Z -> SHIFT
- SW22: value X -> Z
- SW23: value C -> X
- SW24: value V -> C
- SW25: value SHIFT -> V
- SW26: value ALT -> B
- SW27: value B -> N
- SW28: value N -> M
- SW29: value M -> SPACE
- SW30: value SPACE -> ALT
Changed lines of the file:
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@@
 			)
 		)
-		(property "Value" "V"
+		(property "Value" "C"
 			(at -7.81 8.52 0)
 			(layer "F.SilkS")
@@
 			)
 		)
-		(property "Value" "N"
+		(property "Value" "M"
 			(at -7.81 8.52 0)
 			(layer "F.SilkS")
@@
 			)
 		)
-		(property "Value" "C"
+		(property "Value" "X"
 			(at -7.81 8.52 0)
 			(layer "F.SilkS")
@@
 			)
 		)
-		(property "Value" "X"
+		(property "Value" "Z"
 			(at -7.81 8.52 0)
 			(layer "F.SilkS")
@@
 			)
 		)
-		(property "Value" "Z"
+		(property "Value" "SHIFT"
 			(at -7.81 8.52 0)
 			(layer "F.SilkS")
@@
 			)
 		)
-		(property "Value" "SPACE"
+		(property "Value" "ALT"
 			(at -7.81 8.52 0)
 			(layer "F.SilkS")
@@
 			)
 		)
-		(property "Value" "ALT"
+		(property "Value" "B"
 			(at -7.81 8.52 0)
 			(layer "F.SilkS")
@@
 			)
 		)
-		(property "Value" "SHIFT"
+		(property "Value" "V"
 			(at -7.81 8.52 0)
 			(layer "F.SilkS")
@@
 			)
 		)
-		(property "Value" "B"
+		(property "Value" "N"
 			(at -7.81 8.52 0)
 			(layer "F.SilkS")
@@
 			)
 		)
-		(property "Value" "M"
+		(property "Value" "SPACE"
 			(at -7.81 8.52 0)
 			(layer "F.SilkS")
